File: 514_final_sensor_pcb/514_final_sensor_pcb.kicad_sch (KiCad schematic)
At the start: 6 parts, among them SW1 SW_SPDT, U1 MOUDLE-SEEEDUINO-XIAO-ESP32C3

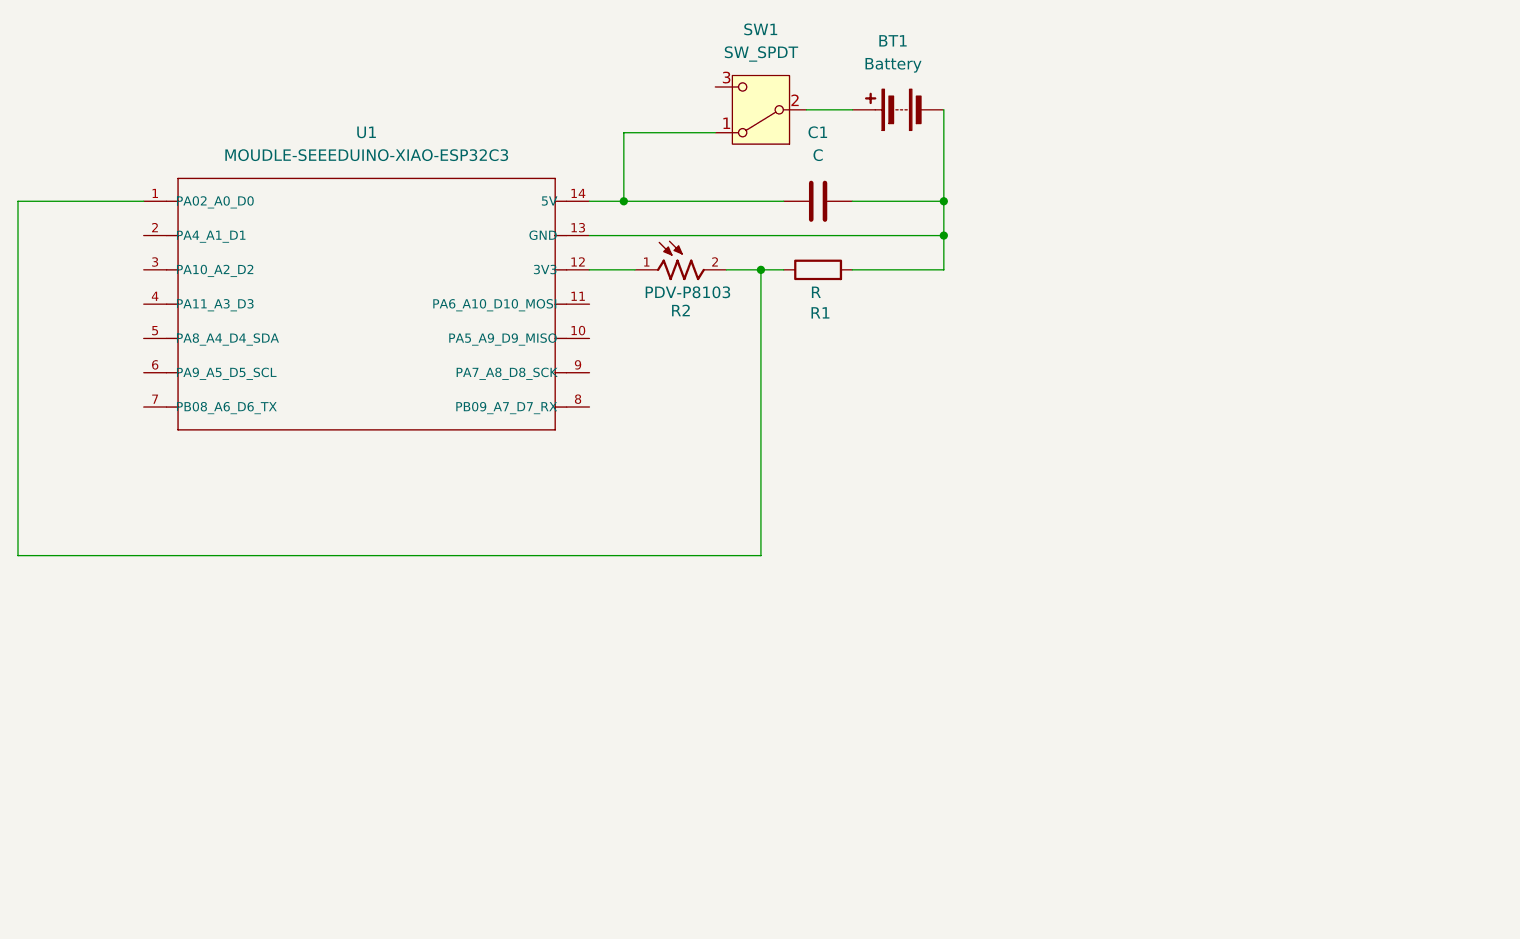
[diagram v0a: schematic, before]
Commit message: battery estimate and datasheet update
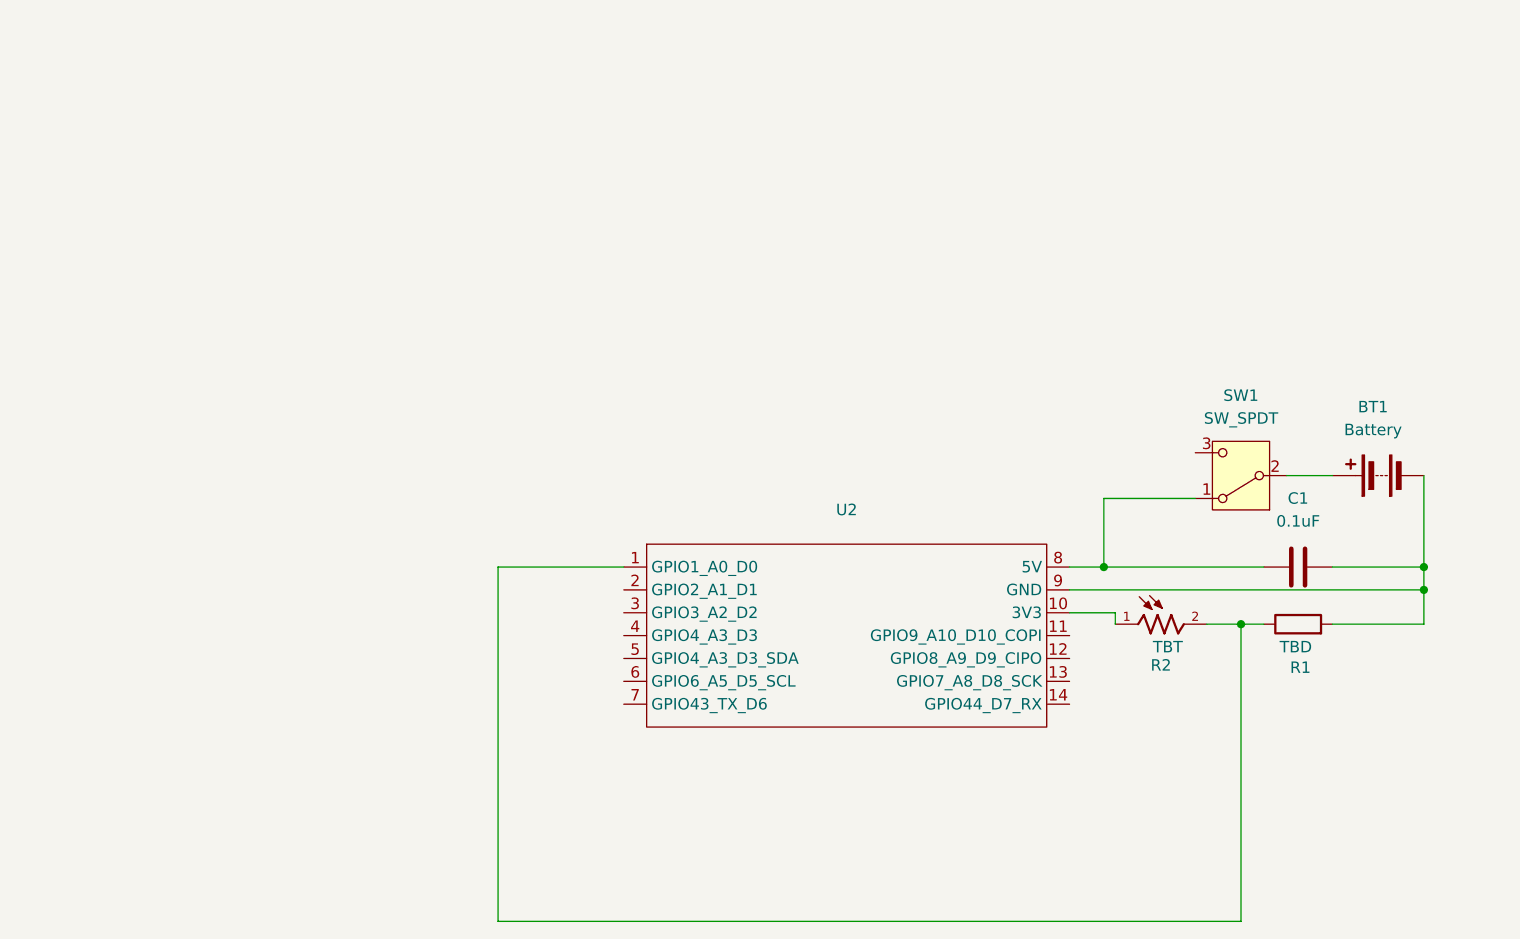
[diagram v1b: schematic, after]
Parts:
- removed U1: MOUDLE-SEEEDUINO-XIAO-ESP32C3, ESP32c3:XIAO_ESP32_SENSE, symbol MOUDLE-SEEEDUINO-XIAO-ESP32C3:MOUDLE-SEEEDUINO-XIAO-ESP32C3
- added U2: ~, ESP32c3:XIAO_ESP32_SENSE, symbol ESP32C3:XIAO_ESP32_SENSE
- C1: value C -> 0.1uF
- R1: value R -> TBD
- R2: value PDV-P8103 -> TBT
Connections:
- net at R1.1, R2.2: now also U2.1 (GPIO1_A0_D0)
- net at R2.1: now also U2.10 (3V3)
- net at BT1.2 (-), C1.2, R1.2: now also U2.9 (GND)
- net at C1.1, SW1.1 (A): now also U2.8 (5V)
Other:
- title: (none) -> Laura_Sensor_Board v1.0
- moved on the sheet: BT1, C1, R1, R2, SW1

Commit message: second device
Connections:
- net GND: now reaches BT1.2 (-), C1.2, R1.2, U2.9 (GND)
